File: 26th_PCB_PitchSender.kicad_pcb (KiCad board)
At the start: 2 copper layers, 120.2 x 28.5 mm, 22 parts, among them J1 Amp, J2 Conn_01x04_Pin, J3 microSD, J4 Conn_01x04_Socket, J5 BNO055, J6 BMP390

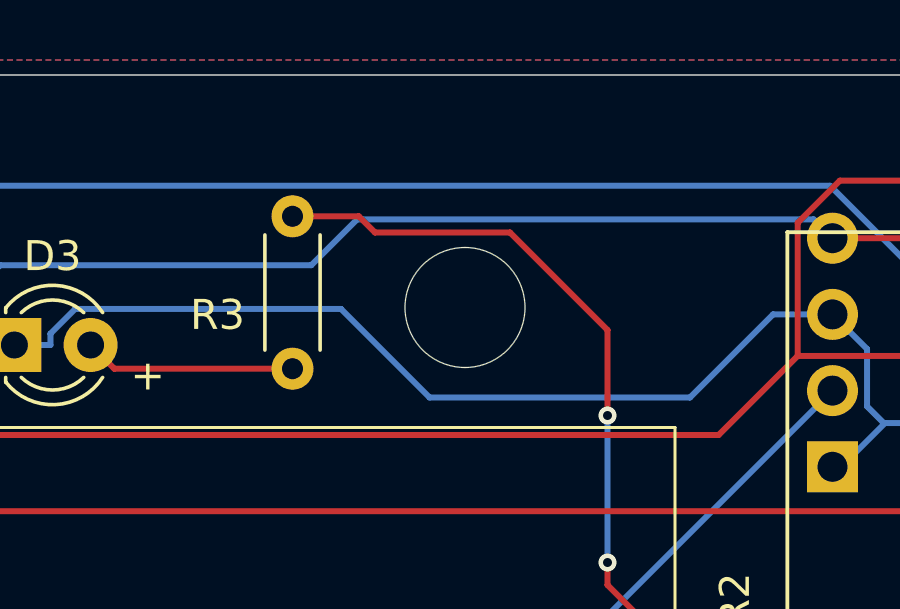
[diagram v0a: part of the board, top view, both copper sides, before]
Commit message: 配線用穴そばの配線ほんのちょっと変更
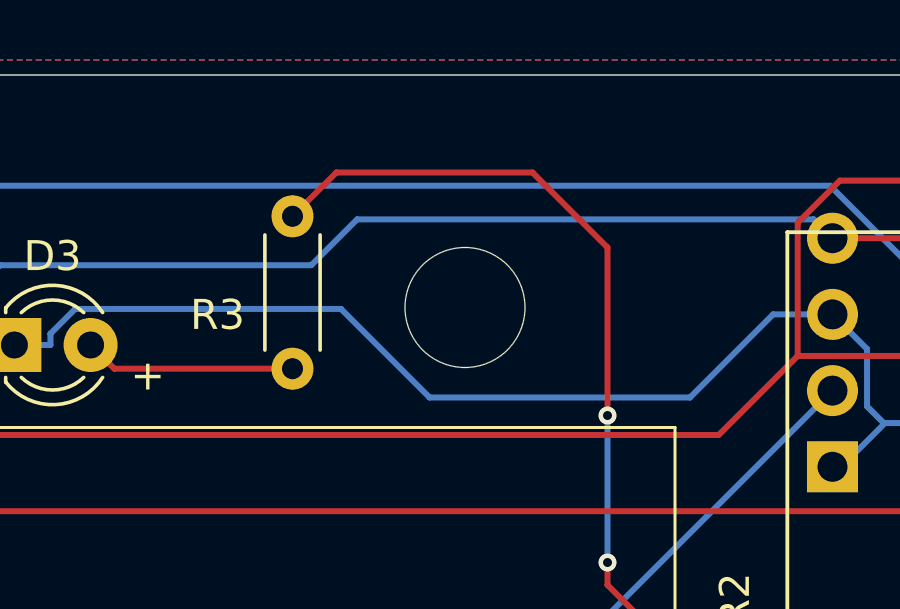
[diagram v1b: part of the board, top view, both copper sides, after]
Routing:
- net Net-(U1-IO25): track 59.0 -> 61.9 mm
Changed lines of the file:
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@@
 	)
 	(segment
-		(start 144.21 81.21)
-		(end 142 81.21)
+		(start 152.5 82.25)
+		(end 152.5 87.85)
 		(width 0.2)
 		(layer "F.Cu")
@@
 	)
 	(segment
-		(start 152.5 85)
-		(end 149.25 81.75)
+		(start 143.46 79.75)
+		(end 150 79.75)
 		(width 0.2)
 		(layer "F.Cu")
@@
 	)
 	(segment
-		(start 144.75 81.75)
-		(end 144.21 81.21)
-		(width 0.2)
-		(layer "F.Cu")
-		(net 37)
-	)
-	(segment
-		(start 149.25 81.75)
-		(end 144.75 81.75)
+		(start 150 79.75)
+		(end 152.5 82.25)
 		(width 0.2)
 		(layer "F.Cu")
@@
 	)
 	(segment
-		(start 152.5 87.85)
-		(end 152.5 85)
+		(start 142 81.21)
+		(end 143.46 79.75)
 		(width 0.2)
 		(layer "F.Cu")

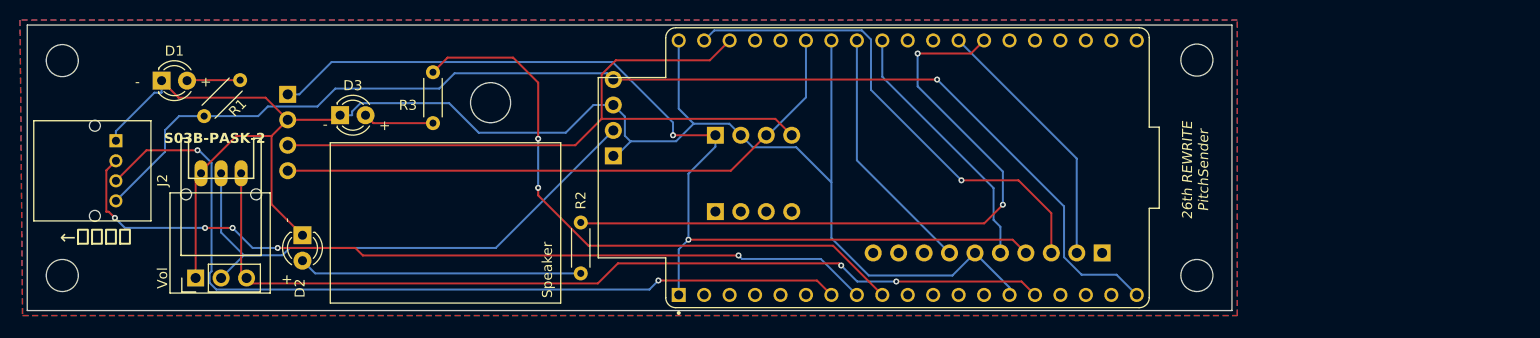
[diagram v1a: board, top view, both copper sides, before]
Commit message: Add IMU
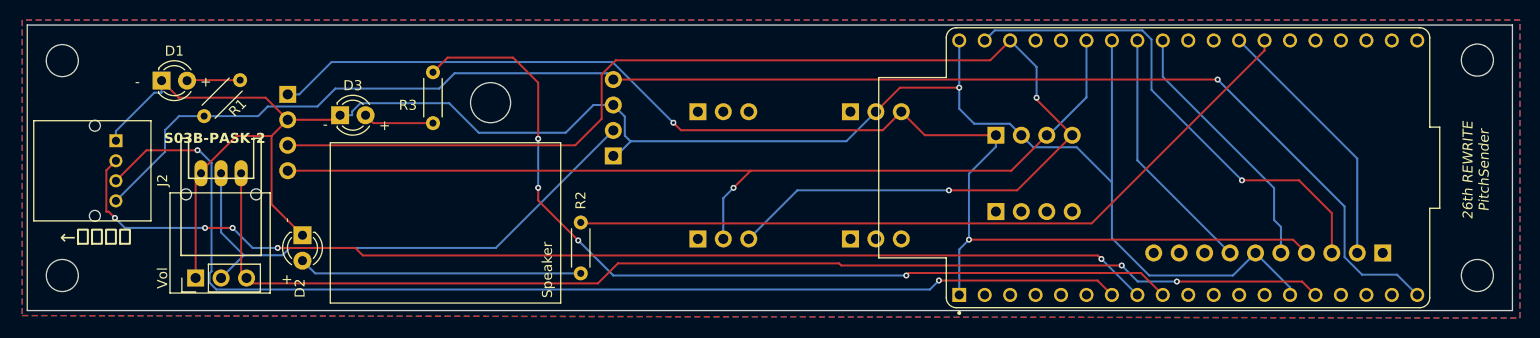
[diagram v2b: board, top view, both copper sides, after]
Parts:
- added J10: Conn_01x03_Socket, Connector_PinSocket_2.54mm:PinSocket_1x03_P2.54mm_Vertical, B.Cu at (183.7, 97.8)
- added J7: Conn_01x03_Socket, Connector_PinSocket_2.54mm:PinSocket_1x03_P2.54mm_Vertical, B.Cu at (168.4, 85.2)
- added J8: Conn_01x03_Socket, Connector_PinSocket_2.54mm:PinSocket_1x03_P2.54mm_Vertical, B.Cu at (183.7, 85.2)
- added J9: Conn_01x03_Socket, Connector_PinSocket_2.54mm:PinSocket_1x03_P2.54mm_Vertical, B.Cu at (168.4, 97.8)
- moved H1 28.0 mm to (246.2, 80.0)
- moved H2 28.0 mm to (246.2, 101.5)
- moved J3 28.0 mm to (236.8, 99.2)
- moved J4 28.0 mm to (198.2, 87.5)
- moved J5 28.0 mm to (198.2, 95.1)
- moved U1 28.0 mm to (217.4, 90.7)
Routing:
- net /SCL: track 70.7 -> 127.6 mm, vias 0 -> 2
- net /SDA: track 60.4 -> 96.4 mm, vias 0 -> 1
- net +3V3: track 99.5 -> 128.3 mm
- net Net-(U1-IO25): track 61.9 -> 90.4 mm, vias 2 -> 4
- net +5V: track 120.6 -> 148.6 mm
- net /BicoTX-psdRX: track 86.7 -> 114.7 mm
- net /SPK: track 91.7 -> 119.7 mm
- net /BicoRX-psdTX: track 83.8 -> 111.8 mm
- net GND: track 175.1 -> 203.1 mm, vias 0 -> 1
- net Net-(U1-IO4): track 68.7 -> 76.4 mm, vias 2 -> 0
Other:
- board size 120.2 x 28.5 mm -> 148.2 x 28.5 mm
- board text added: "AE-LSM6DSV16X"
